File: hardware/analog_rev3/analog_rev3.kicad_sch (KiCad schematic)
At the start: 202 parts, among them J1 Jack, J10 Jack, J11 Jack, J12 Jack, J13 Jack, J14 Jack, J15 Jack, J16 Jack, J17 Jack, J18 Jack, J19 Jack, J2 Jack, J20 Jack, J21 OLED Display, J22 Conn_02x07, J23 Conn_02x07, J24 Trigger Inputs, J25 Trigger Inputs, J26 Conn_01x16, J27 Conn_01x16, J3 Jack, J4 Jack, J5 Jack, J6 Jack, J7 Jack, J8 Jack, J9 Jack, SW1 SW_Push, SW2 SW_Push, SW3 SW_Push, SW4 SW_Push, SW5 SW_Push, SW6 Encoder, SW7 Encoder, U1 LM339, U10 MCP6022, U11 LM833, U2 MCP6002, U3 MCP6002, U4 MCP6002, U5 MCP6002, U6 OPA2172, U7 OPA2172, U8 OPA2172, U9 OPA2172

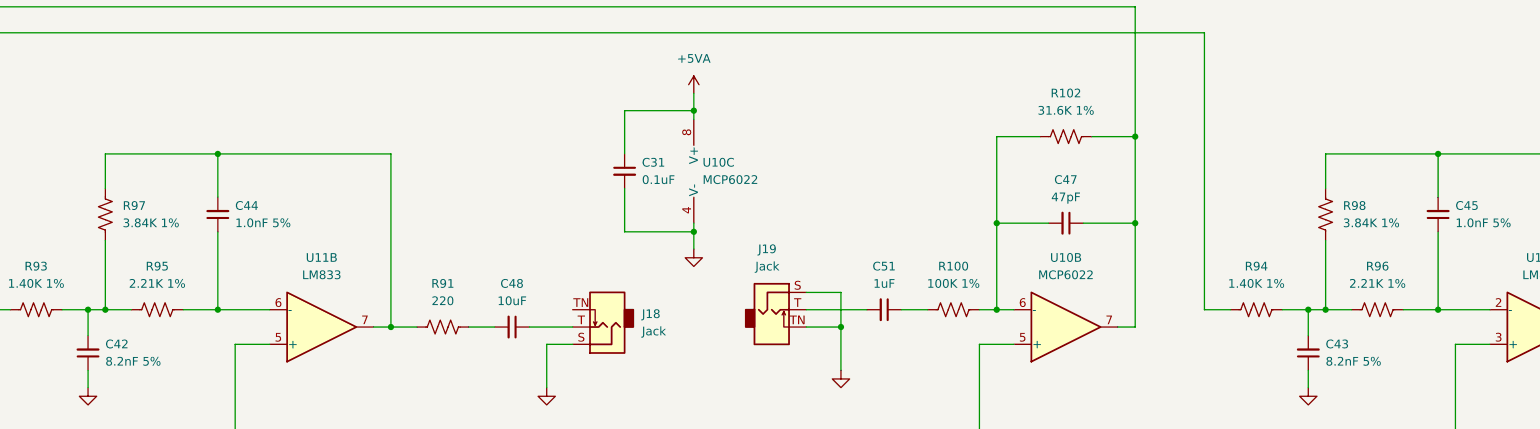
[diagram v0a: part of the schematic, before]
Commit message: fixed R97-98 value typo. was 3.84k, is now 3.48k
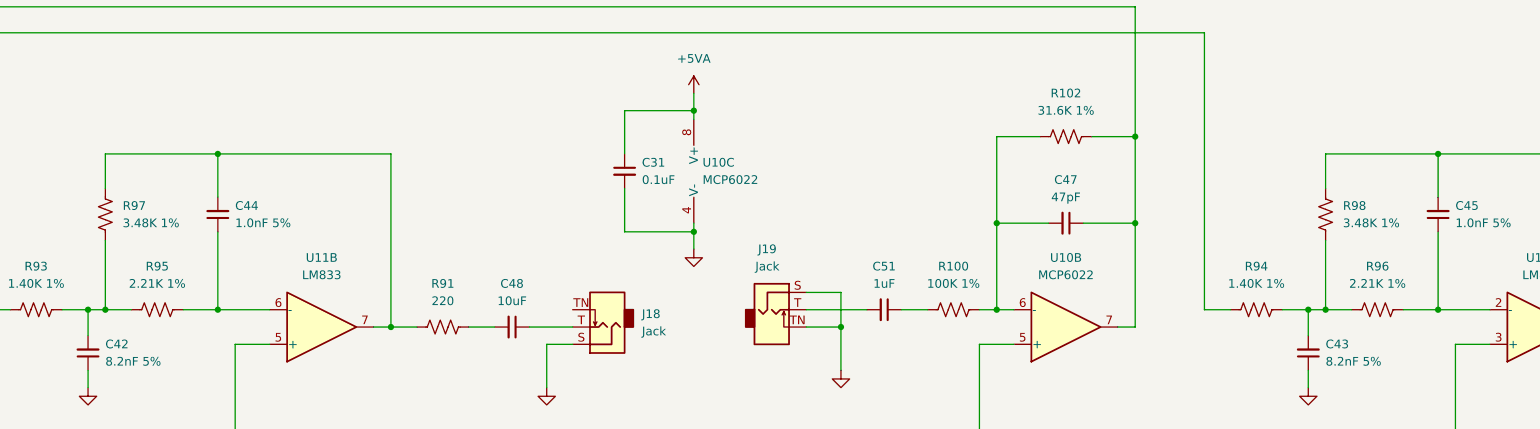
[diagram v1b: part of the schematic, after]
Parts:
- R97, R98: value 3.84K 1% -> 3.48K 1%
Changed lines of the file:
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@@
 		(fields_autoplaced yes)
 		(property "Reference" "R98"
-			(at 313.69 466.09 0)
+			(at 313.69 466.0899 0)
 			(effects
 				(font
@@
 			)
 		)
-		(property "Value" "3.84K 1%"
-			(at 313.69 468.63 0)
+		(property "Value" "3.48K 1%"
+			(at 313.69 468.6299 0)
 			(effects
 				(font
@@
 		(fields_autoplaced yes)
 		(property "Reference" "R97"
-			(at 134.62 466.09 0)
+			(at 134.62 466.0899 0)
 			(effects
 				(font
@@
 			)
 		)
-		(property "Value" "3.84K 1%"
-			(at 134.62 468.63 0)
+		(property "Value" "3.48K 1%"
+			(at 134.62 468.6299 0)
 			(effects
 				(font
